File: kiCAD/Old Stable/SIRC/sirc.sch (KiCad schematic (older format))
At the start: 5 parts, among them IC1 STM8S003F3P, J1 DB25, P1 CONN_01X04

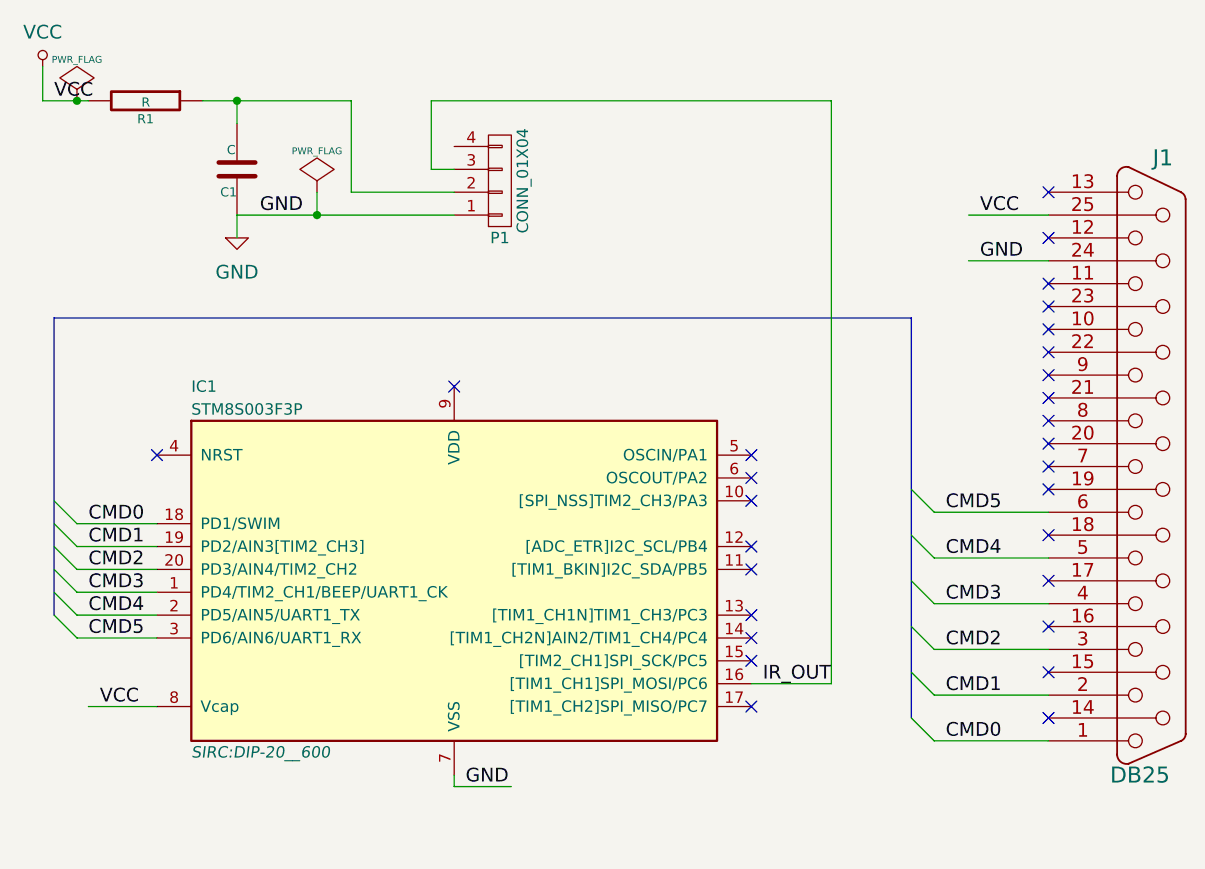
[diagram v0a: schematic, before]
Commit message: Revision 2, fix DB25 female -> male
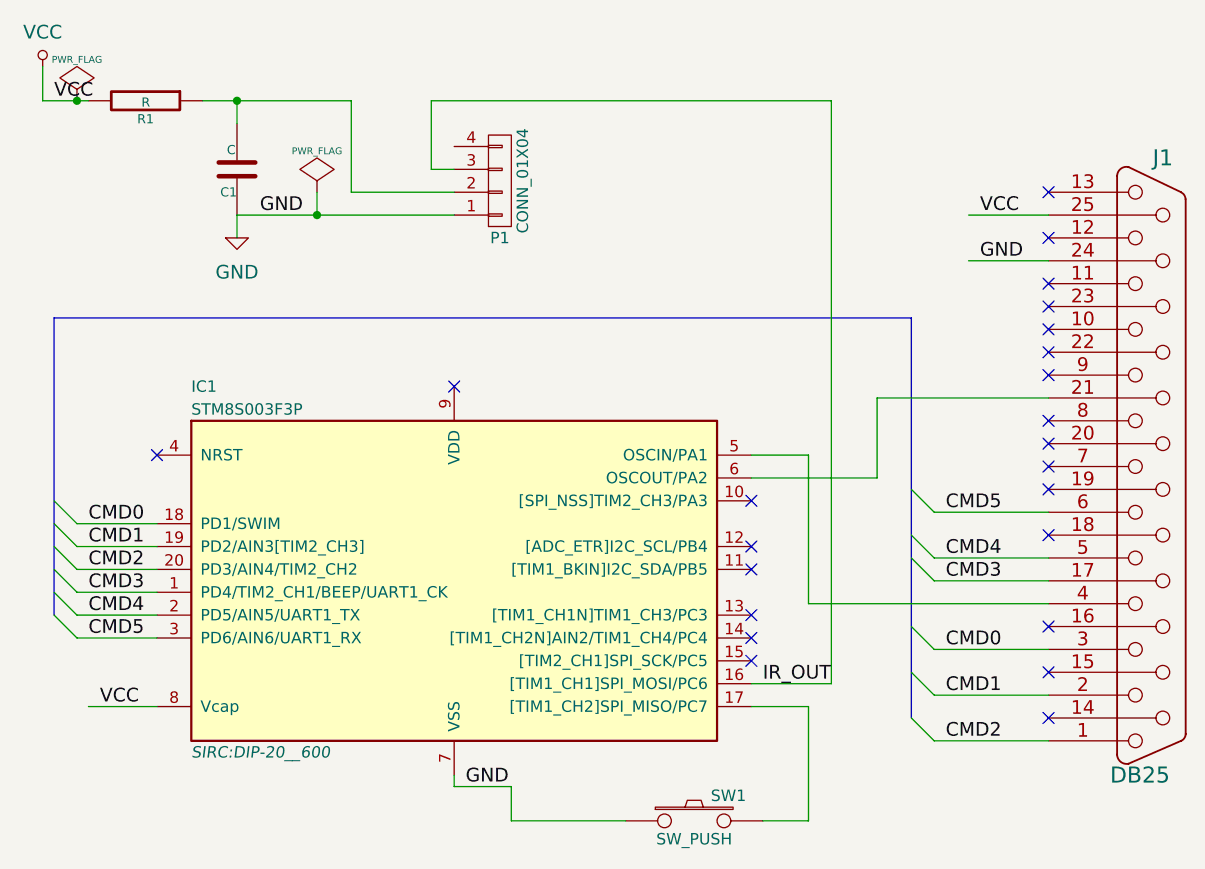
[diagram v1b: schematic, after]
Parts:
- added SW1: SW_PUSH, ~, symbol SW_PUSH
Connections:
- wire segments 31 -> 42
- no-connect marks 28 -> 23
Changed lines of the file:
@@
 LIBS:valves
 LIBS:stm8
+LIBS:tsop
+LIBS:st-microelectronics
 LIBS:sirc-cache
 EELAYER 27 0
@@
 Sheet 1 1
 Title ""
-Date "11 may 2015"
+Date "16 may 2015"
 Rev ""
 Comp ""
@@
 	8200 4900 8300 5000
 Entry Wire Line
-	8200 4700 8300 4800
+	8200 4600 8300 4700
 Entry Wire Line
 	8200 4500 8300 4600
@@
 	8300 4600 8800 4600
 Wire Wire Line
-	8300 4800 8800 4800
+	7750 4800 8800 4800
 Wire Wire Line
 	8300 5000 8800 5000
@@
 	8300 5400 8800 5400
 Text Label 8350 5400 0    60   ~ 0
-CMD0
+CMD2
 Text Label 8350 5200 0    60   ~ 0
 CMD1
 Text Label 8350 5000 0    60   ~ 0
-CMD2
-Text Label 8350 4800 0    60   ~ 0
+CMD0
+Text Label 8350 4700 0    60   ~ 0
 CMD3
 Text Label 8350 4600 0    60   ~ 0
@@
 Text Label 7550 5150 0    60   ~ 0
 IR_OUT
-NoConn ~ 7500 4150
-NoConn ~ 7500 4250
 NoConn ~ 7500 4350
 NoConn ~ 7500 4550
@@
 NoConn ~ 7500 4950
 NoConn ~ 7500 5050
-NoConn ~ 7500 5250
 NoConn ~ 4900 4150
 NoConn ~ 6200 3850
@@
 NoConn ~ 8800 3700
 NoConn ~ 8800 3800
-NoConn ~ 8800 3900
 NoConn ~ 8800 4000
 NoConn ~ 8800 4100
@@
 NoConn ~ 8800 4300
 NoConn ~ 8800 4500
-NoConn ~ 8800 4700
 NoConn ~ 8800 4900
 NoConn ~ 8800 5100
@@
 Wire Wire Line
 	7850 2600 7850 5150
+Wire Wire Line
+	8800 3900 8050 3900
+Wire Wire Line
+	8050 3900 8050 4250
+Wire Wire Line
+	8050 4250 7500 4250
+Wire Wire Line
+	7750 4150 7750 4800
+Wire Wire Line
+	7750 4150 7500 4150
+$Comp
+L SW_PUSH SW1
+U 1 1 555689CB
+P 7250 5750
+F 0 "SW1" H 7400 5860 50  0000 C CNN
+F 1 "SW_PUSH" H 7250 5670 50  0000 C CNN
+F 2 "~" H 7250 5750 60  0000 C CNN
+F 3 "~" H 7250 5750 60  0000 C CNN
+	1    7250 5750
+	1    0    0    -1
+$EndComp
+Wire Wire Line
+	7500 5250 7750 5250
+Wire Wire Line
+	7750 5250 7750 5750
+Wire Wire Line
+	7750 5750 7550 5750
+Wire Wire Line
+	6450 5600 6450 5750
+Wire Wire Line
+	6450 5750 6950 5750
+Wire Wire Line
+	8800 4700 8300 4700
 $EndSCHEMATC
